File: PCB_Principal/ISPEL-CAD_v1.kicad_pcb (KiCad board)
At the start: 2 copper layers, 130 x 160 mm, 171 parts, among them J1 Vin, J10 E1, J11 S1, J12 E2, J13 S2, J14 FRENTE, J15 PRUEBA_5V, J2 GND_NUCLEO, J3 CN8_NUCLEO, J4 CN9_NUCLEO, J5 GND_NUCLEO, J6 GND_NUCLEO, J7 CN7_NUCLEO, J8 CN10_NUCLEO, J9 GND_NUCLEO, Q201 BC807, Q202 BC559C, Q203 BC549C, Q204 BC549C, Q205 BC559C, Q206 2SD882, Q207 2SB772, Q251 BC807, Q252 BC559C, Q253 BC549C, Q254 BC549C, Q255 BC559C, Q256 2SD882, Q257 2SB772, U1 LM350_TO220, U101 TL071, U151 TL071, U2 LM350_TO220, U201 LM318, U251 LM318, U3 LM337_TO220, U301 TLV3501AID, U4 LM1117DT-5.0, U5 TL431DBZ

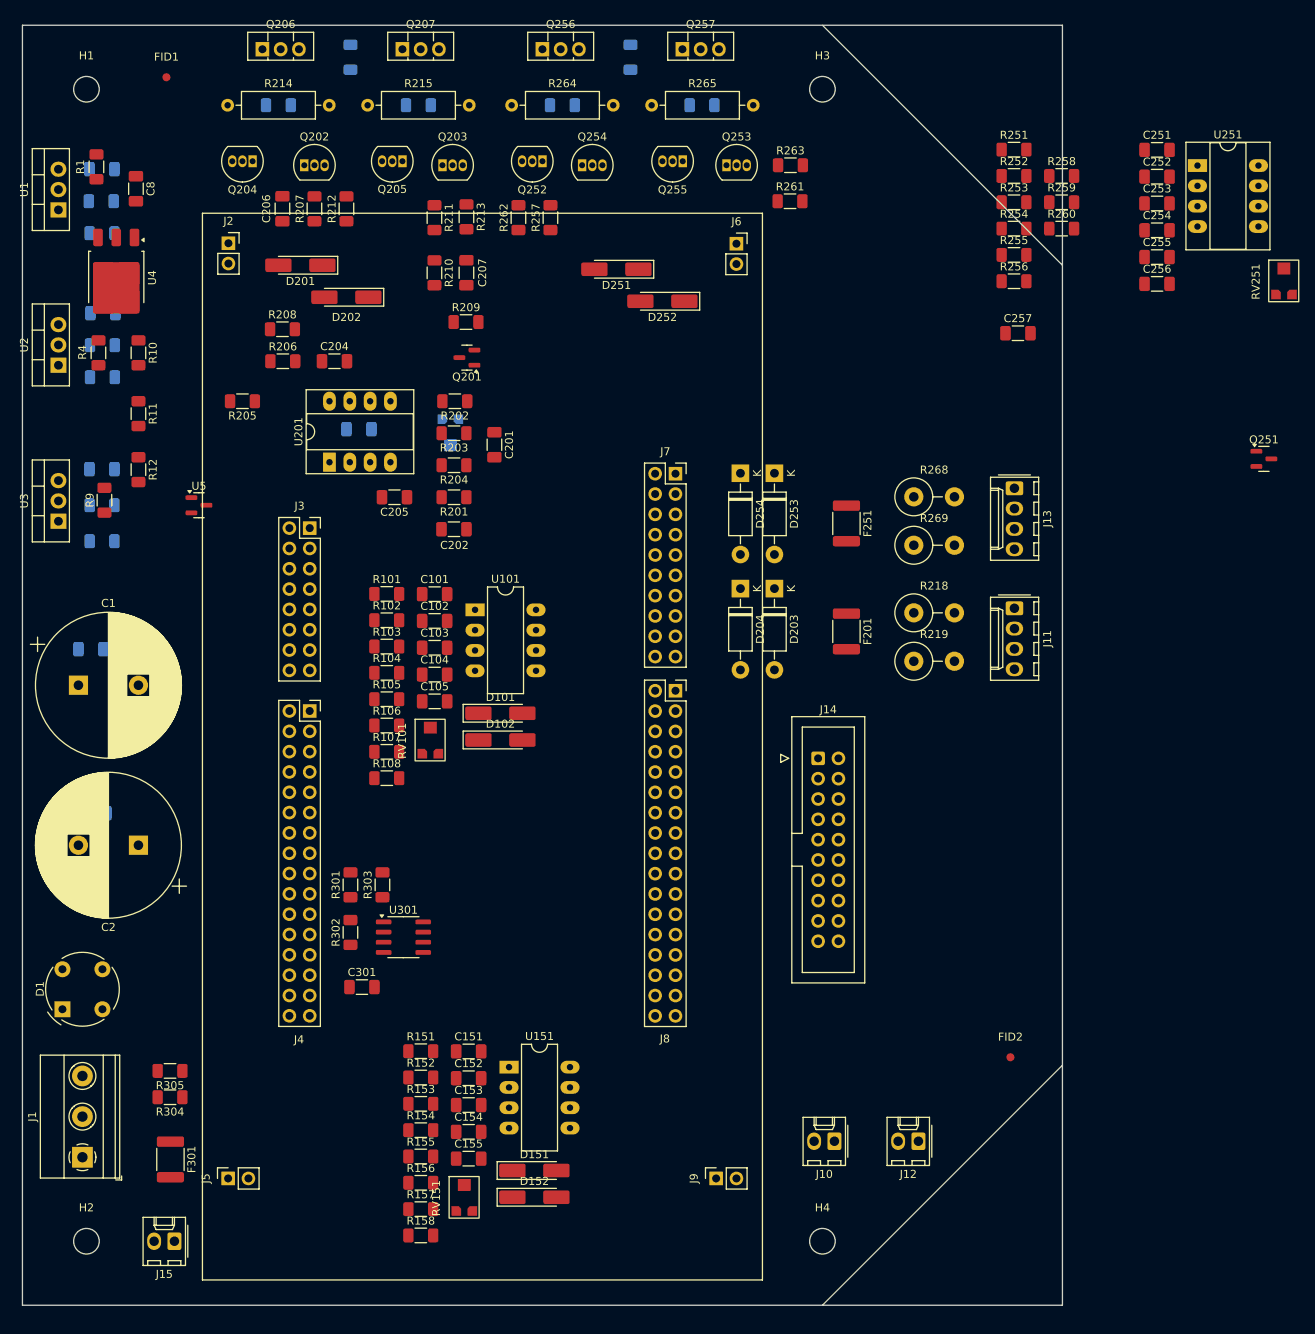
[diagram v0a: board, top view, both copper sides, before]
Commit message: Placa con conector J8.
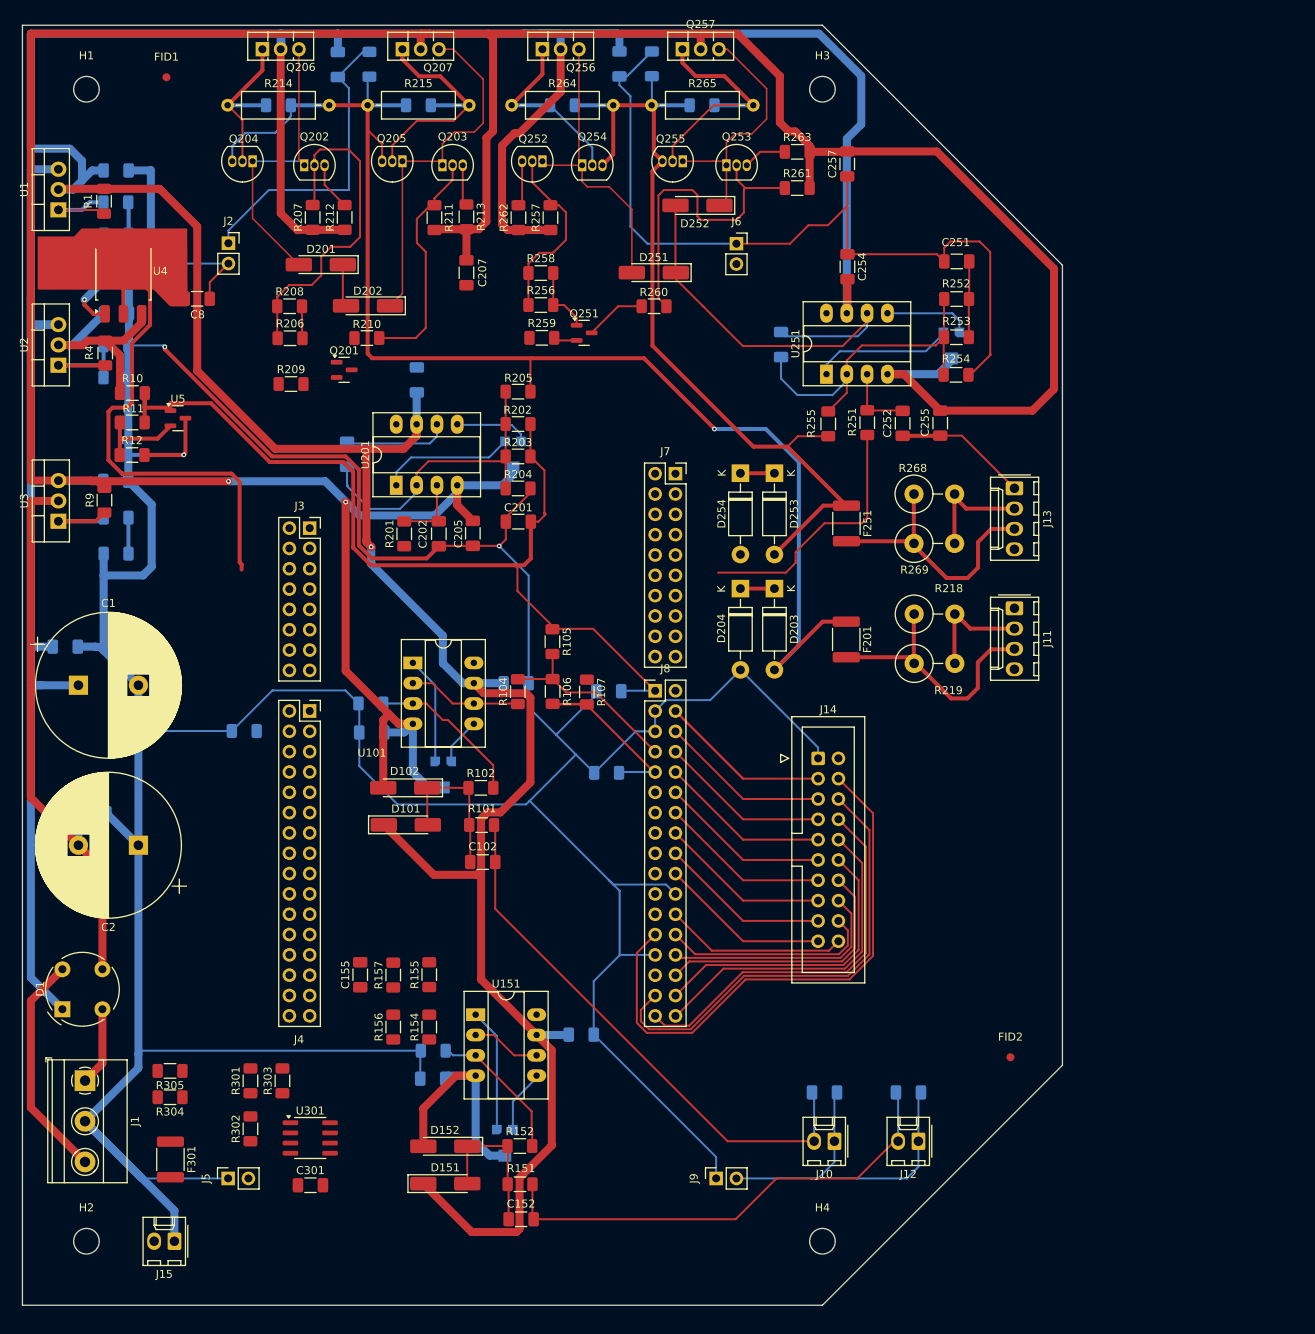
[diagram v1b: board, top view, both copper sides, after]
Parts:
- C101, C103, C104, C105, C151, C153, C154, C204, C206, C253, C256, R103, R108, R153, R158, RV101, RV151, RV251: moved to B.Cu
- J8: footprint Connector_PinSocket_2.54mm:PinSocket_2x17_P2.54mm_Vertical -> Libreria_ISPEL:PinSocket_2x17_P2.54mm_Vertical_impar-par
- U101, U151: footprint Package_DIP:CERDIP-8_W7.62mm_SideBrazed_LongPads -> Package_DIP:CERDIP-8_W7.62mm_SideBrazed_LongPads_Socket
- moved Q251 86.4 mm to (100.2, 68.5)
- moved C101 79.1 mm to (130.3, 163.4)
- moved C256 72.6 mm to (104.6, 34.8), turned to -90 degrees
- moved R259 67.1 mm to (94.9, 69.1)
- moved R158 66.8 mm to (57.7, 118.2), turned to 180 degrees
- moved R258 66.2 mm to (94.8, 61.0)
- moved R256 59.2 mm to (94.8, 65.0)
- moved C151 55.2 mm to (140.8, 163.4)
- moved U251 53.2 mm to (130.5, 73.6), turned to 90 degrees
- moved R260 51.9 mm to (109.0, 65.1), turned to 180 degrees
- moved C253 50.2 mm to (124.8, 69.9), turned to 90 degrees
- moved C252 44.3 mm to (140.0, 79.8), turned to -90 degrees
- moved RV251 42.3 mm to (146.1, 70.0)
- moved C254 39.0 mm to (133.1, 60.2), turned to -90 degrees
- moved R251 38.7 mm to (135.6, 79.7), turned to 90 degrees
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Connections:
- net Net-(J14-Pin_10) renamed /LED4
- net Net-(J14-Pin_11) renamed /BTN5
- net Net-(J14-Pin_12) renamed /LED5
- net Net-(J14-Pin_13) renamed /BTN6
- net Net-(J14-Pin_14) renamed /LED6
- net Net-(J14-Pin_15) renamed /BTN7
- net Net-(J14-Pin_16) renamed /LED7
- net Net-(J14-Pin_17) renamed /BTN8
- net Net-(J14-Pin_18) renamed /LED8
- net Net-(J14-Pin_19) renamed /BTN9
- net Net-(J14-Pin_20) renamed /LED9
- net Net-(J14-Pin_3) renamed /BTN1
- net Net-(J14-Pin_4) renamed /LED1
- net Net-(J14-Pin_5) renamed /BTN2
- net Net-(J14-Pin_6) renamed /LED2
- net Net-(J14-Pin_7) renamed /BTN3
- net Net-(J14-Pin_8) renamed /LED3
- net Net-(J14-Pin_9) renamed /BTN4
- RV101 pad 2: GND -> VEE
- RV151 pad 2: GND -> VEE
- RV201 pad 1: Net-(U201-BAL3) -> Net-(U201-BAL1)
- RV201 pad 2: GND -> VEE
- RV201 pad 3: Net-(U201-BAL1) -> Net-(U201-BAL3)
- RV251 pad 1: Net-(U251-BAL3) -> Net-(U251-BAL1)
- RV251 pad 2: GND -> VEE
- RV251 pad 3: Net-(U251-BAL1) -> Net-(U251-BAL3)
- U101 pad 1: Net-(RV101-Pad3) -> Net-(RV101-Pad1)
- U101 pad 5: Net-(RV101-Pad1) -> Net-(RV101-Pad3)
- U151 pad 1: Net-(RV151-Pad3) -> Net-(RV151-Pad1)
- U151 pad 5: Net-(RV151-Pad1) -> Net-(RV151-Pad3)
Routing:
- net GND: track 0.00 -> 773.7 mm, vias 0 -> 4
- net VCC: track 0.00 -> 487.4 mm, vias 0 -> 1
- net VEE: track 0.00 -> 457.7 mm, vias 0 -> 2
- net /Salida 1/SALIDA0: track 0.00 -> 171.6 mm, vias 0 -> 1
- net /Fuente/VP: track 0.00 -> 134.0 mm
- net V33REF: track 0.00 -> 127.8 mm
- net /Salida 2/SALIDA0: track 0.00 -> 107.0 mm
- net /LED1: track 0.00 -> 69.9 mm
- net /Fuente/VN: track 0.00 -> 69.9 mm
- net E1: track 0.00 -> 68.6 mm
- net V5: track 0.00 -> 68.3 mm
- net E2: track 0.00 -> 60.2 mm
- net /LED2: track 0.00 -> 57.8 mm
- net /Salida 2/VOA: track 0.00 -> 52.1 mm
- net /LED3: track 0.00 -> 48.7 mm
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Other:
- outline, holes or cut-outs redrawn

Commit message: Placa PCB con ERC. Falta huella de portafusibles.
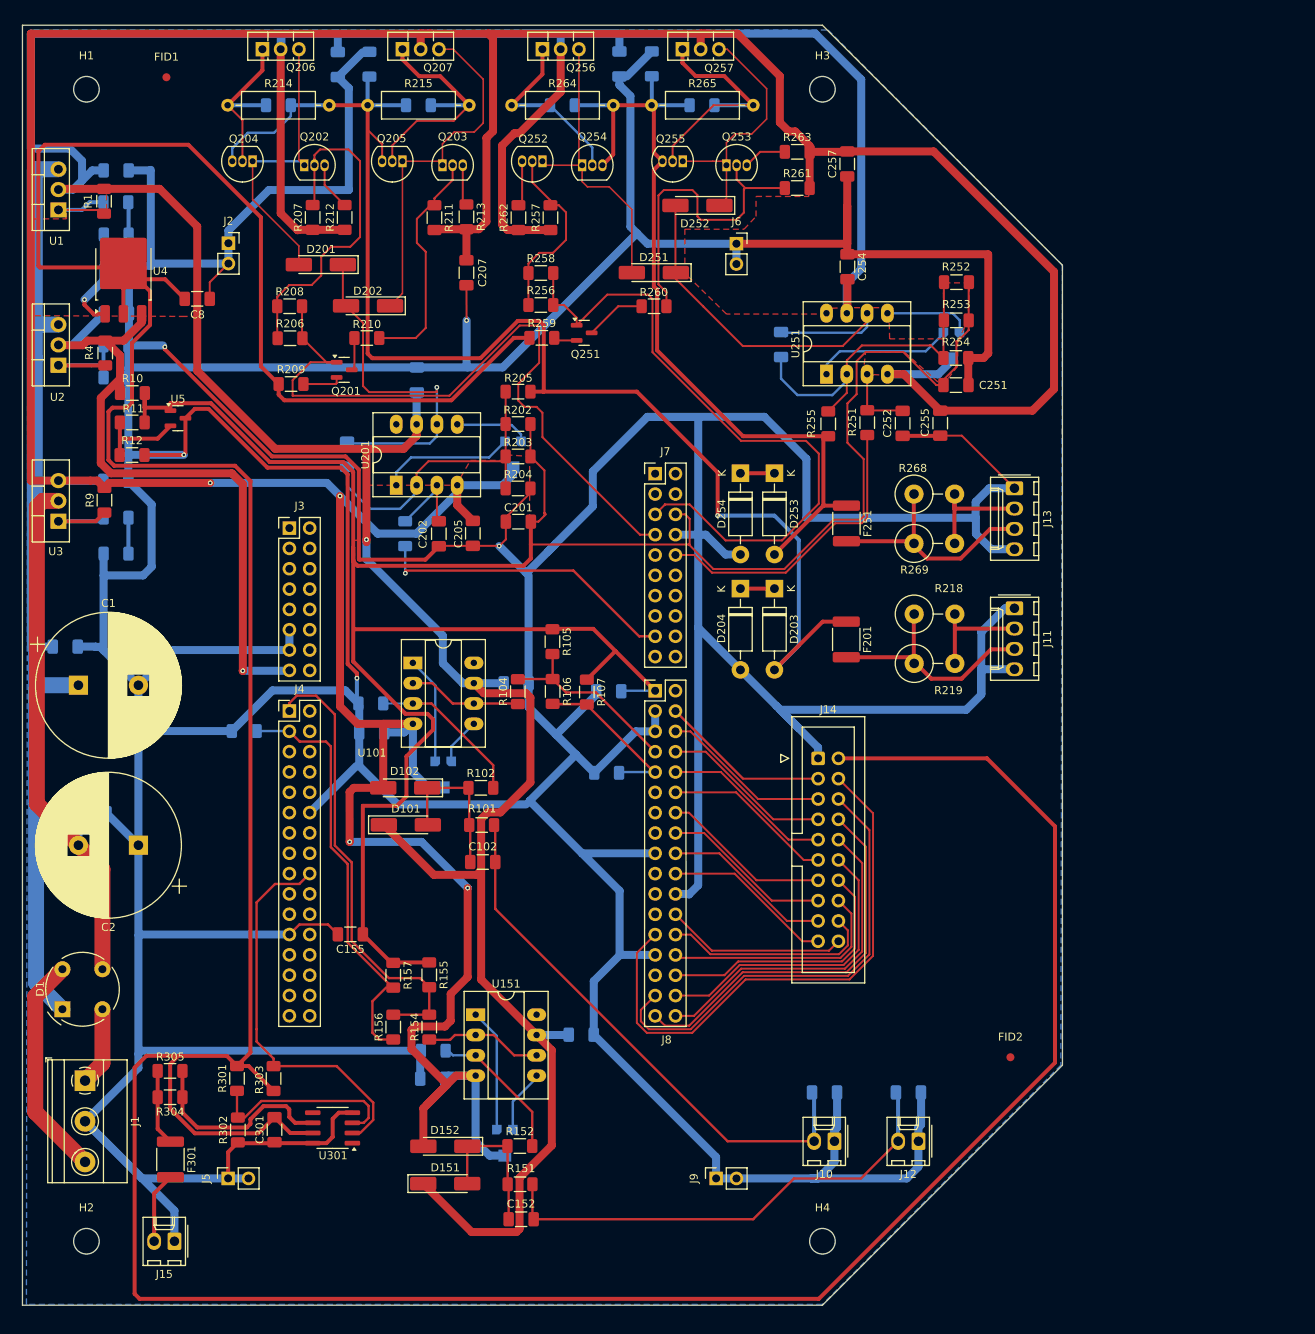
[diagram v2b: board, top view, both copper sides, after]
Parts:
- J3: footprint Connector_PinSocket_2.54mm:PinSocket_2x08_P2.54mm_Vertical -> Libreria_ISPEL:PinSocket_2x08_P2.54mm_Vertical_impar-par
- J4: footprint Connector_PinSocket_2.54mm:PinSocket_2x16_P2.54mm_Vertical -> Libreria_ISPEL:PinSocket_2x16_P2.54mm_Vertical_impar-par
- J7: footprint Connector_PinSocket_2.54mm:PinSocket_2x10_P2.54mm_Vertical -> Libreria_ISPEL:PinSocket_2x10_P2.54mm_Vertical_impar-par
- R201: moved to B.Cu
- moved C251 15.5 mm to (146.7, 75.0), turned to 0 degrees
- moved C301 8.27 mm to (61.5, 168.1), turned to 90 degrees
- moved C155 5.20 mm to (71.0, 143.6), turned to 180 degrees
- moved U301 3.06 mm to (68.8, 167.8), turned to 180 degrees
- moved J3 2.54 mm to (63.4, 92.9)
- moved J4 2.54 mm to (63.4, 115.7)
- moved J7 2.54 mm to (109.1, 86.1)
- moved R253 2.11 mm to (146.7, 66.9)
- moved R254 2.11 mm to (146.7, 71.6)
- moved R252 2.11 mm to (146.8, 62.1)
- moved R301 1.71 mm to (56.8, 161.7)
- moved R302 1.58 mm to (56.9, 168.1)
- moved R303 1.15 mm to (61.4, 161.7), turned to -90 degrees
- moved R201 0.12 mm to (77.8, 93.6)
- turned R157 to -90 degrees
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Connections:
- J3 pad 7: V33 -> unconnected-(J3-Pin_7-Pad7)
- R209 pad 1: V33 -> V5
- R259 pad 1: V33 -> V5
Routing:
- net GND: track 773.7 -> 1215.0 mm, vias 4 -> 6
- net V5: track 68.3 -> 509.4 mm
- net V33REF: track 127.8 -> 308.7 mm
- net CTRL_S1: track 4.02 -> 88.6 mm
- net CTRL_S2: track 8.55 -> 83.5 mm
- net VEE: track 457.7 -> 525.2 mm, vias 2 -> 4
- net V7: track 27.3 -> 86.9 mm, vias 0 -> 1
- net ADC2_C10: track 0.00 -> 57.3 mm
- net ADC2_C20: track 0.00 -> 53.7 mm
- net PRUEBA: track 0.00 -> 49.3 mm
- net DAC1: track 0.00 -> 38.4 mm, vias 0 -> 1
- net /Salida 1/VOA: track 18.5 -> 44.2 mm, vias 0 -> 1
- net Net-(R304-Pad1): track 0.00 -> 25.2 mm
- net Net-(U301-+): track 0.00 -> 24.5 mm
- net /Fuente/VP: track 134.0 -> 119.6 mm
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- added copper zone on B.Cu, net GND
- added copper zone on F.Cu, net GND
- added copper zone on F.Cu, net V5

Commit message: PCB con huella de portafusibles 1808.
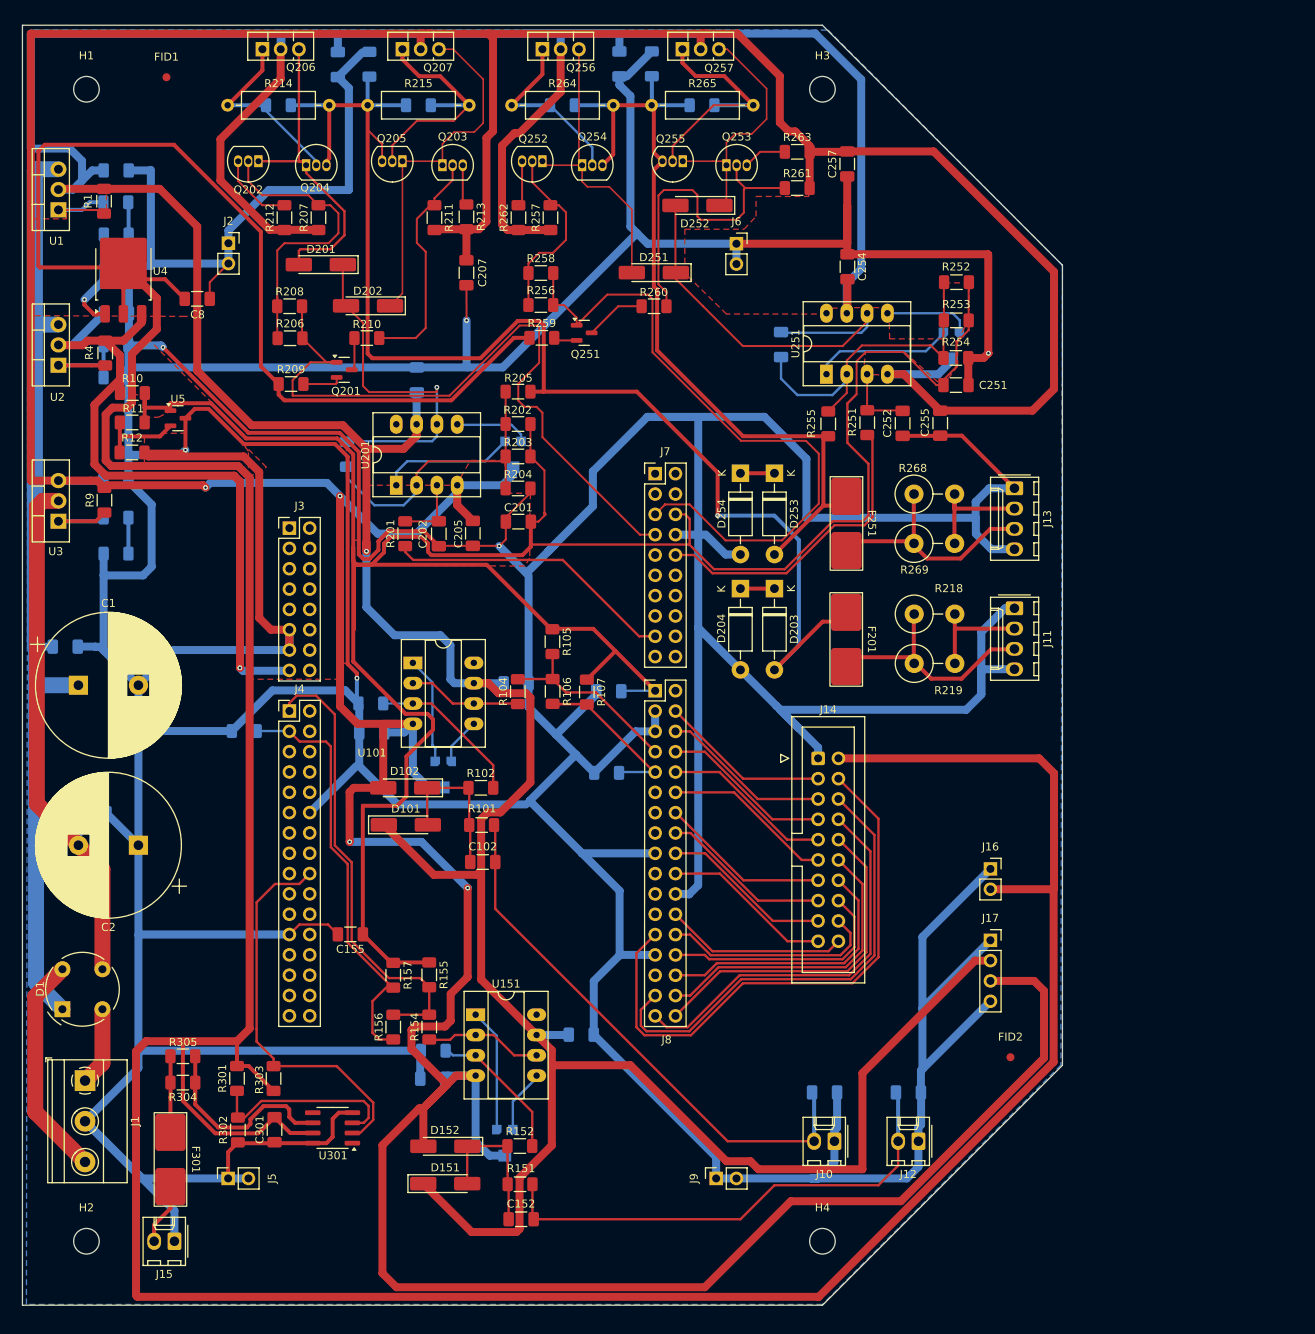
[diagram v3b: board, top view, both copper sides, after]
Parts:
- added J16: V5, Connector_PinSocket_2.54mm:PinSocket_1x02_P2.54mm_Vertical, F.Cu at (151.0, 135.5)
- added J17: VREG, Connector_PinSocket_2.54mm:PinSocket_1x04_P2.54mm_Vertical, F.Cu at (151.0, 144.4)
- F201, F251, F301: footprint Fuse:Fuse_1812_4532Metric_Pad1.30x3.40mm_HandSolder -> Libreria_ISPEL:Fuseholder_1808_handsoldering
- R201: moved to F.Cu
- moved R212 7.53 mm to (62.8, 54.0)
- moved Q204 6.71 mm to (65.5, 47.5), turned to 0 degrees
- moved Q202 5.75 mm to (59.5, 47.0), turned to 180 degrees
- moved R304 2.43 mm to (50.0, 162.2)
- moved R305 2.43 mm to (50.0, 158.9)
- moved R207 0.73 mm to (67.0, 54.0)
- moved R12 0.32 mm to (43.7, 83.4)
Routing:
- net VEE: track 525.2 -> 659.4 mm
- net GND: track 1215.0 -> 1315.9 mm, vias 6 -> 7
- net VCC: track 487.3 -> 574.4 mm
- net V33REF: track 308.7 -> 324.4 mm
- net V5: track 509.4 -> 521.4 mm
- net Net-(Q202-B): track 43.3 -> 38.6 mm
- net /Salida 1/SALIDA0: track 174.9 -> 170.6 mm
- net Net-(Q202-E): track 6.01 -> 9.51 mm
- net Net-(Q204-B): track 21.4 -> 23.7 mm
- net /Salida 1/VBP: track 37.5 -> 39.5 mm
- net DAC1: track 38.4 -> 36.4 mm, vias 1 -> 0
- net E2: track 60.2 -> 62.0 mm
- net /LED1: track 69.9 -> 71.6 mm
- net /LED2: track 57.8 -> 59.3 mm
- net Net-(U201-+): track 10.8 -> 9.35 mm
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- added copper zone on F.Cu, net V33REF
